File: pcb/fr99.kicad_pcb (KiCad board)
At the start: 2 copper layers, 100 x 79.9 mm, 21 parts, among them M1 SD, P1 CONN_02X18, SW2 RESET, U1 541, U2 541, U3 541, U4 377, U5 62256, U6 8515

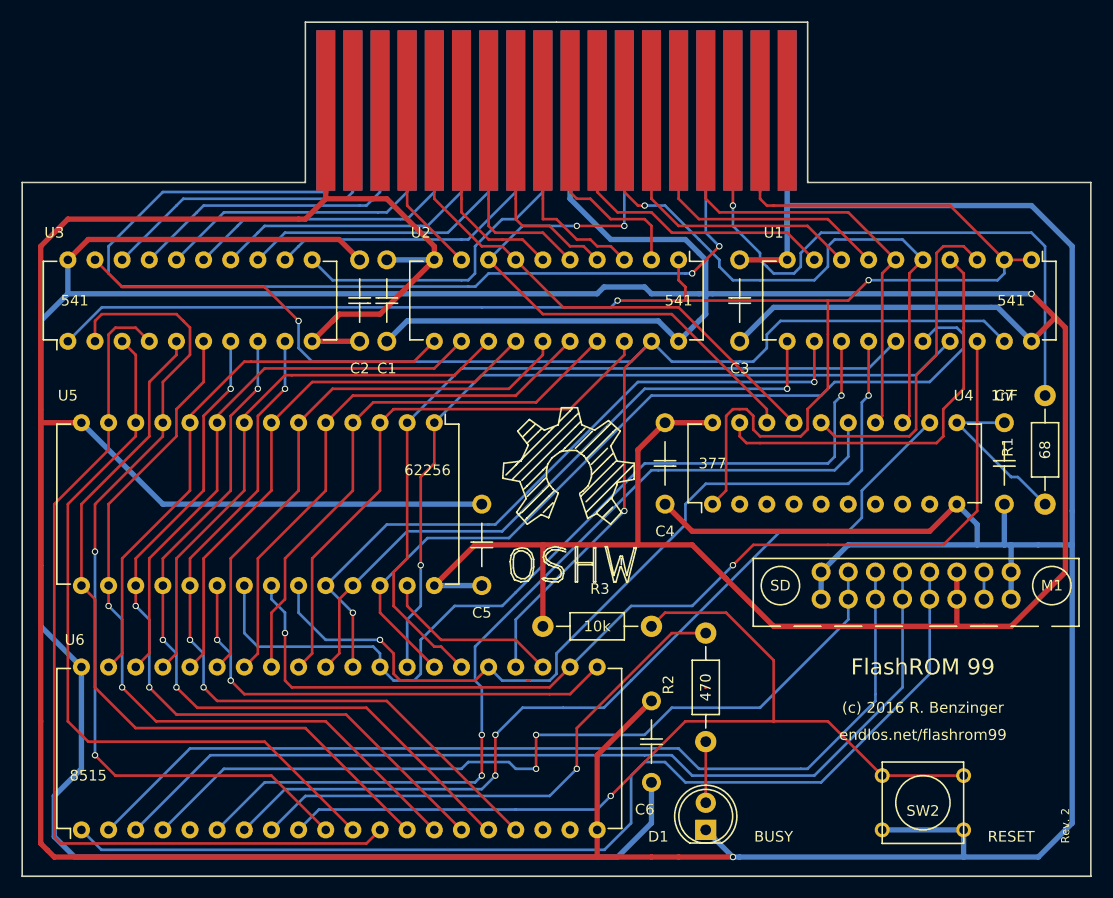
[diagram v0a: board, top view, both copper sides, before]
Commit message: Initial conversion to KiCad 9
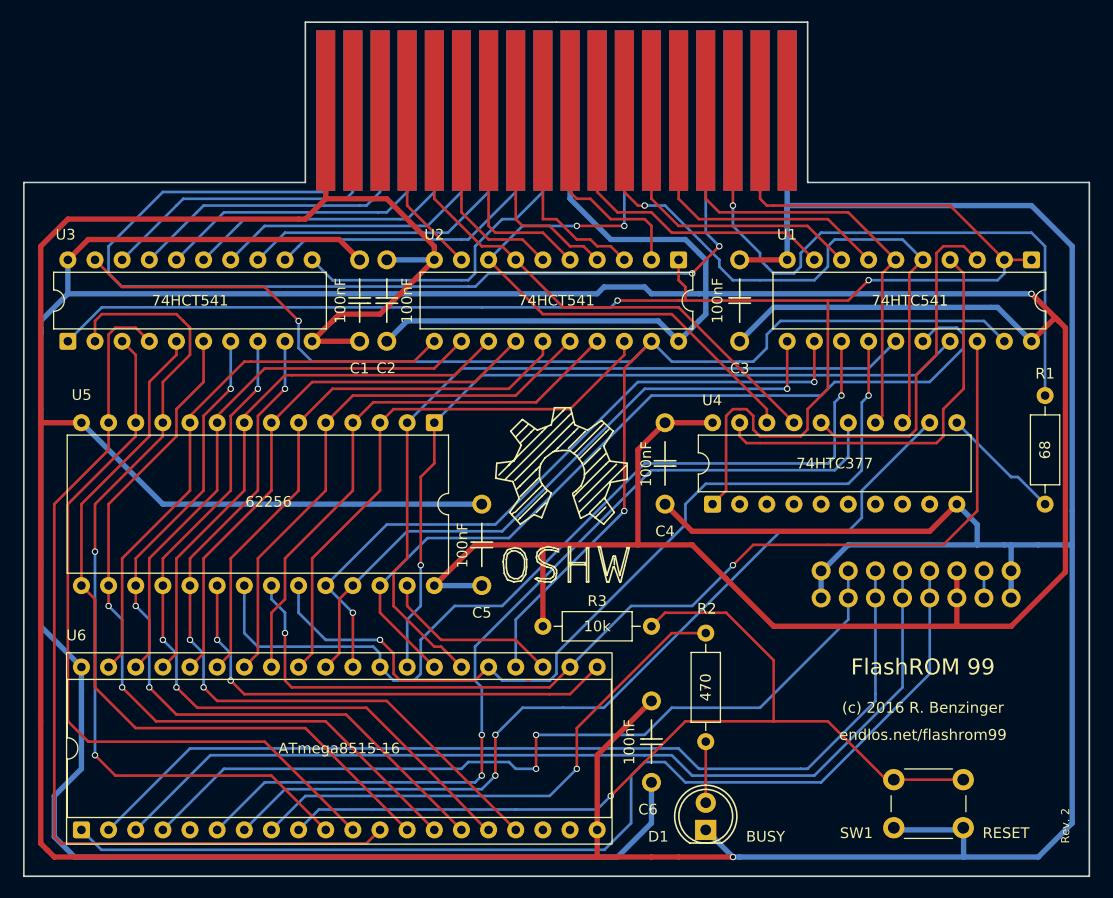
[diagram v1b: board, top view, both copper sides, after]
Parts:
- removed C7: 1nF, flashcart-footprints:C_C
- M1: moved to B.Cu
- R1, R2, R3: footprint Resistors_ThroughHole:Resistor_Horizontal_RM10mm -> Resistor_THT:R_Axial_DIN0207_L6.3mm_D2.5mm_P10.16mm_Horizontal
- SW1: renamed from SW2; footprint Buttons_Switches_ThroughHole:SW_PUSH_SMALL -> Button_Switch_THT:SW_PUSH_6mm_H5mm
- U1: value 541 -> 74HTC541; footprint Housings_DIP:DIP-20_W7.62mm -> Package_DIP:DIP-20_W7.62mm
- U2, U3: value 541 -> 74HCT541; footprint Housings_DIP:DIP-20_W7.62mm -> Package_DIP:DIP-20_W7.62mm
- U4: value 377 -> 74HTC377; footprint Housings_DIP:DIP-20_W7.62mm -> Package_DIP:DIP-20_W7.62mm
- U5: footprint Housings_DIP:DIP-28_W15.24mm -> Package_DIP:DIP-28_W15.24mm
- U6: value 8515 -> ATmega8515-16; footprint Housings_DIP:DIP-40_W15.24mm -> Package_DIP:DIP-40_W15.24mm_Socket
- moved M1 4.97 mm to (161.9, 87.5)
- moved SW1 4.44 mm to (181.6, 107.8)
- moved REF** 0.66 mm to (144.1, 55.2)
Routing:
- net GND: track 475.6 -> 470.8 mm
- net Net-(C7-Pad1): track 16.0 -> 11.5 mm
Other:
- board size 100 x 79.9 mm -> 99.7 x 79.9 mm
- net class Default removed
- net class Power removed

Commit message: Cleanup footprints and library links
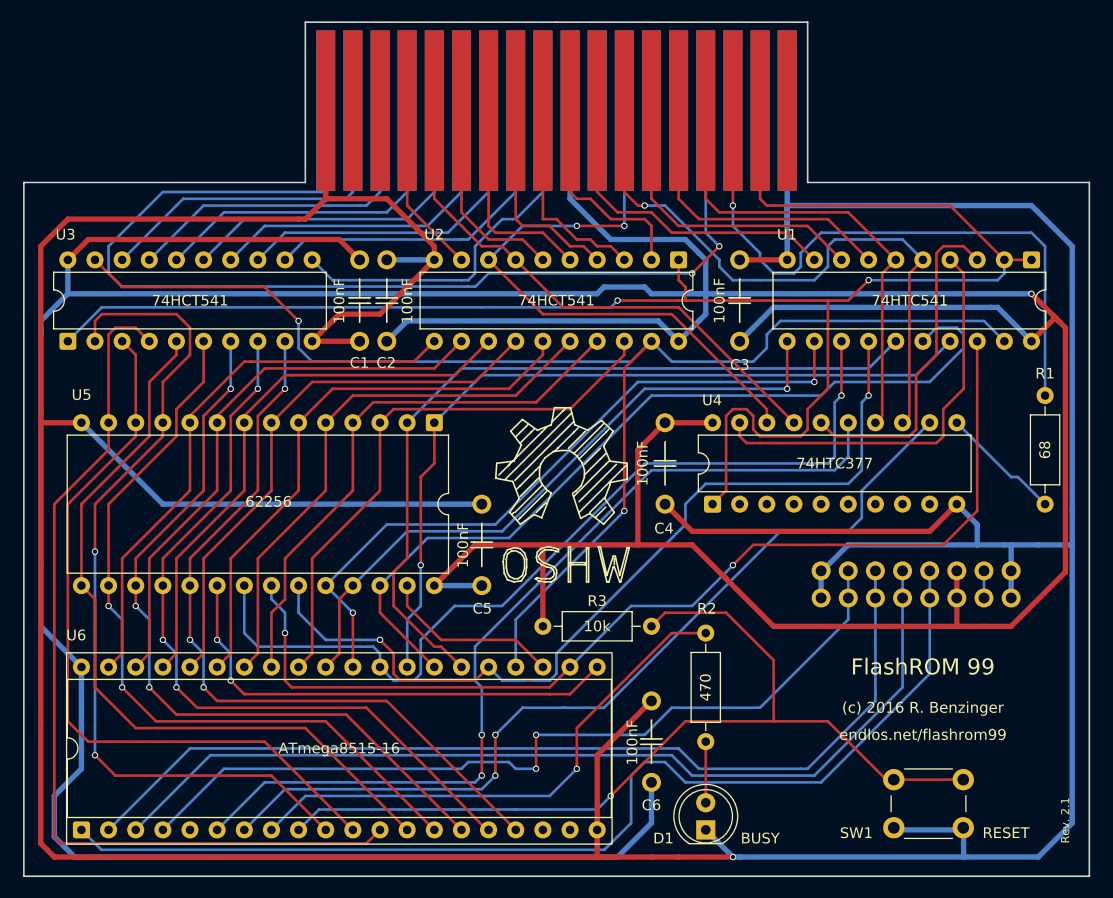
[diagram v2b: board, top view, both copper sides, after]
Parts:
- C1, C2, C3, C4, C5, C6: footprint flashcart-footprints:C_C -> fr99-footprints:C_C
- D1: footprint LEDs:LED-5MM -> LED_THT:LED_D5.0mm
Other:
- board text added: "Rev. 2.1"
- board text removed: "Rev. 2"
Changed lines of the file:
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@@
 	(net 84 "Net-(U6-Pad19)")
 	(net 85 "Net-(P1-Pad32)")
-	(footprint "LEDs:LED-5MM"
+	(footprint "LED_THT:LED_D5.0mm"
 		(layer "F.Cu")
 		(at 157.48 107.95 90)
-		(descr "LED 5mm round vertical")
-		(tags "LED 5mm round vertical")
+		(descr "LED, diameter 5.0mm, 2 pins, http://cdn-reichelt.de/documents/datenblatt/A500/LL-504BC2E-009.pdf, generated by kicad-footprint-generator")
+		(tags "LED")
 		(property "Reference" "D1"
-			(at -0.635 -4.445 180)
+			(at -0.8 -3.96 180)
 			(layer "F.SilkS")
 			(effects
@@
 		)
 		(property "Value" "BUSY"
-			(at -0.635 5.595 180)
+			(at -0.8 5.095 180)
 			(layer "F.SilkS")
 			(effects
@@
 		(attr through_hole)
 		(fp_line
-			(start -1.23 1.5)
-			(end -1.23 -1.5)
+			(start -1.29 -1.545)
+			(end -1.29 1.545)
 			(stroke
-				(width 0.15)
+				(width 0.12)
 				(type solid)
 			)
@@
 		)
 		(fp_arc
-			(start -1.23 -1.5)
-			(mid 4.18544 -0.014565)
-			(end -1.214888 1.524904)
+			(start -1.29 -1.54483)
+			(mid 2.071779 -2.880495)
+			(end 4.26 0)
 			(stroke
-				(width 0.15)
+				(width 0.12)
+				(type solid)
+			)
+			(layer "F.SilkS")
+		)
+		(fp_arc
+			(start 4.26 0)
+			(mid 2.071779 2.880495)
+			(end -1.29 1.54483)
+			(stroke
+				(width 0.12)
 				(type solid)
 			)
@@
 		(fp_circle
 			(center 1.27 0)
-			(end 0.97 -2.5)
+			(end 3.77 0)
 			(stroke
-				(width 0.15)
+				(width 0.12)
 				(type solid)
 			)
@@
 		)
 		(fp_line
-			(start -1.5 -1.55)
-			(end -1.5 1.55)
+			(start 4.49 -3.21)
+			(end -1.94 -3.21)
 			(stroke
 				(width 0.05)
@@
 			(layer "F.CrtYd")
 		)
-		(fp_arc
-			(start -1.498248 -1.55316)
-			(mid 4.50039 0.001807)
-			(end -1.5 1.55)
+		(fp_line
+			(start -1.94 -3.21)
+			(end -1.94 3.21)
+			(stroke
+				(width 0.05)
+				(type solid)
+			)
+			(layer "F.CrtYd")
+		)
+		(fp_line
+			(start 4.49 3.21)
+			(end 4.49 -3.21)
 			(stroke
 				(width 0.05)
@@
 			(layer "F.CrtYd")
 		)
+		(fp_line
+			(start -1.94 3.21)
+			(end 4.49 3.21)
+			(stroke
+				(width 0.05)
+				(type solid)
+			)
+			(layer "F.CrtYd")
+		)
+		(fp_line
+			(start -1.23 -1.469694)
+			(end -1.23 1.469694)
+			(stroke
+				(width 0.1)
+				(type solid)
+			)
+			(layer "F.Fab")
+		)
+		(fp_arc
+			(start -1.23 -1.469694)
+			(mid 4.17 0)
+			(end -1.23 1.469694)
+			(stroke
+				(width 0.1)
+				(type solid)
+			)
+			(layer "F.Fab")
+		)
+		(fp_circle
+			(center 1.27 0)
+			(end 3.77 0)
+			(stroke
+				(width 0.1)
+				(type solid)
+			)
+			(fill no)
+			(layer "F.Fab")
+		)
+		(fp_text user "${REFERENCE}"
+			(at 1.27 0 180)
+			(layer "F.Fab")
+			(effects
+				(font
+					(size 0.8 0.8)
+					(thickness 0.12)
+				)
+			)
+		)
 		(pad "1" thru_hole rect
-			(at 0 0 180)
-			(size 2 1.9)
-			(drill 1.00076)
-			(layers "*.Cu" "*.Mask" "F.SilkS")
+			(at 0 0 90)
+			(size 1.8 1.8)
+			(drill 0.9)
+			(layers "*.Cu" "*.Mask")
 			(remove_unused_layers no)
 			(net 1 "GND")
@@
 		(pad "2" thru_hole circle
 			(at 2.54 0 90)
-			(size 1.9 1.9)
-			(drill 1.00076)
-			(layers "*.Cu" "*.Mask" "F.SilkS")
+			(size 1.8 1.8)
+			(drill 0.9)
+			(layers "*.Cu" "*.Mask")
 			(remove_unused_layers no)
 			(net 3 "Net-(D1-Pad2)")
 		)
 		(embedded_fonts no)
-		(model "LEDs.3dshapes/LED-5MM.wrl"
+		(model "${KICAD9_3DMODEL_DIR}/LED_THT.3dshapes/LED_D5.0mm.step"
 			(offset
-				(xyz 1.269999981 0 0)
+				(xyz 0 0 0)
 			)
 			(scale
@@
 			)
 			(rotate
-				(xyz 0 0 90)
+				(xyz 0 0 0)
 			)
 		)
@@
 		)
 	)
-	(footprint "flashcart-footprints:C_C"
+	(footprint "fr99-footprints:C_C"
 		(layer "F.Cu")
 		(at 125.095 62.23 90)
 		(property "Reference" "C1"
-			(at -2.54 -0.02 180)
+			(at -2.02 -0.02 180)
 			(layer "F.SilkS")
 			(effects
@@
 		)
 		(property "Value" "100nF"
-			(at 3.795022 -1.80653 90)
+			(at 3.768283 -1.899181 90)
 			(layer "F.SilkS")
 			(effects
@@
 		(embedded_fonts no)
 	)
-	(footprint "flashcart-footprints:C_C"
+	(footprint "fr99-footprints:C_C"
 		(layer "F.Cu")
 		(at 127.635 54.61 -90)
 		(property "Reference" "C2"
-			(at 10.14 0.06 0)
+			(at 9.64 0.06 0)
 			(layer "F.SilkS")
 			(effects
@@
 		)
 		(property "Value" "100nF"
-			(at 3.824978 -1.893053 90)
+			(at 3.846744 -1.927317 270)
 			(layer "F.SilkS")
 			(effects
@@
 		)
 		(property "Datasheet" ""
-			(at 0 0 90)
+			(at 0 0 270)
 			(layer "F.Fab")
 			(hide yes)
@@
 		)
 		(property "Description" ""
-			(at 0 0 90)
+			(at 0 0 270)
 			(layer "F.Fab")
 			(hide yes)
@@
 		(embedded_fonts no)
 	)
-	(footprint "flashcart-footprints:C_C"
+	(footprint "fr99-footprints:C_C"
 		(layer "F.Cu")
 		(at 160.655 54.61 -90)
 		(property "Reference" "C3"
-			(at 10.16 0 0)
+			(at 9.826573 -0.010898 0)
 			(layer "F.SilkS")
 			(effects
@@
 		)
 		(property "Value" "100nF"
-			(at 3.81 2.08 90)
+			(at 3.825818 1.887016 270)
 			(layer "F.SilkS")
 			(effects
@@
 		)
 		(property "Datasheet" ""
-			(at 0 0 90)
+			(at 0 0 270)
 			(layer "F.Fab")
 			(hide yes)
@@
 		)
 		(property "Description" ""
-			(at 0 0 90)
+			(at 0 0 270)
 			(layer "F.Fab")
 			(hide yes)
@@
 		(embedded_fonts no)
 	)
-	(footprint "flashcart-footprints:C_C"
+	(footprint "fr99-footprints:C_C"
 		(layer "F.Cu")
 		(at 153.67 77.47 90)
 		(property "Reference" "C4"
-			(at -2.54 0 180)
+			(at -2.28 -0.095 180)
 			(layer "F.SilkS")
 			(effects
@@
 		)
 		(property "Value" "100nF"
-			(at 3.748492 -1.768754 90)
+			(at 3.81 -2.095 90)
 			(layer "F.SilkS")
 			(effects
@@
 		(embedded_fonts no)
 	)
-	(footprint "flashcart-footprints:C_C"
+	(footprint "fr99-footprints:C_C"
 		(layer "F.Cu")
 		(at 136.525 77.47 -90)
 		(property "Reference" "C5"
-			(at 10.16 0 0)
+			(at 9.78 -0.05 0)
 			(layer "F.SilkS")
 			(effects
@@
 		)
 		(property "Value" "100nF"
-			(at 3.855976 1.81089 90)
+			(at 3.842483 1.75249 270)
 			(layer "F.SilkS")
 			(effects
@@
 		)
 		(property "Datasheet" ""
-			(at 0 0 90)
+			(at 0 0 270)
 			(layer "F.Fab")
 			(hide yes)
@@
 		)
 		(property "Description" ""
-			(at 0 0 90)
+			(at 0 0 270)
 			(layer "F.Fab")
 			(hide yes)
@@
 		(embedded_fonts no)
 	)
-	(footprint "flashcart-footprints:C_C"
+	(footprint "fr99-footprints:C_C"
 		(layer "F.Cu")
 		(at 152.4 95.885 -90)
 		(property "Reference" "C6"
-			(at 10.16 0.325 0)
+			(at 9.754869 0.002019 0)
 			(layer "F.SilkS")
 			(effects
@@
 		)
 		(property "Value" "100nF"
-			(at 3.846005 2.071925 90)
+			(at 3.893666 1.78829 270)
 			(layer "F.SilkS")
 			(effects
@@
 		)
 		(property "Datasheet" ""
-			(at 0 0 90)
+			(at 0 0 270)
 			(layer "F.Fab")
 			(hide yes)
@@
 		)
 		(property "Description" ""
-			(at 0 0 90)
+			(at 0 0 270)
 			(layer "F.Fab")
 			(hide yes)
@@
 		)
 	)
-	(gr_text "Rev. 2"
+	(gr_text "Rev. 2.1"
 		(at 191.135 109.22 90)
 		(layer "F.SilkS")
